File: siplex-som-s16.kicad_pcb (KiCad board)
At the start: 8 copper layers, 30 x 30 mm, 58 parts, among them J1 RFShield_OnePiece, J5 Conn_01x22, J7 Conn_01x22, J8 Conn_01x22, J9 Conn_01x22, U1 STM32H743IIKx, U2 IS42S16160J-6BLI, U3 W25Q32JVZP, U4 AP2112K-3.3, U5 W25Q32JVZP, Y1 25MHz, Y2 32.768KHz

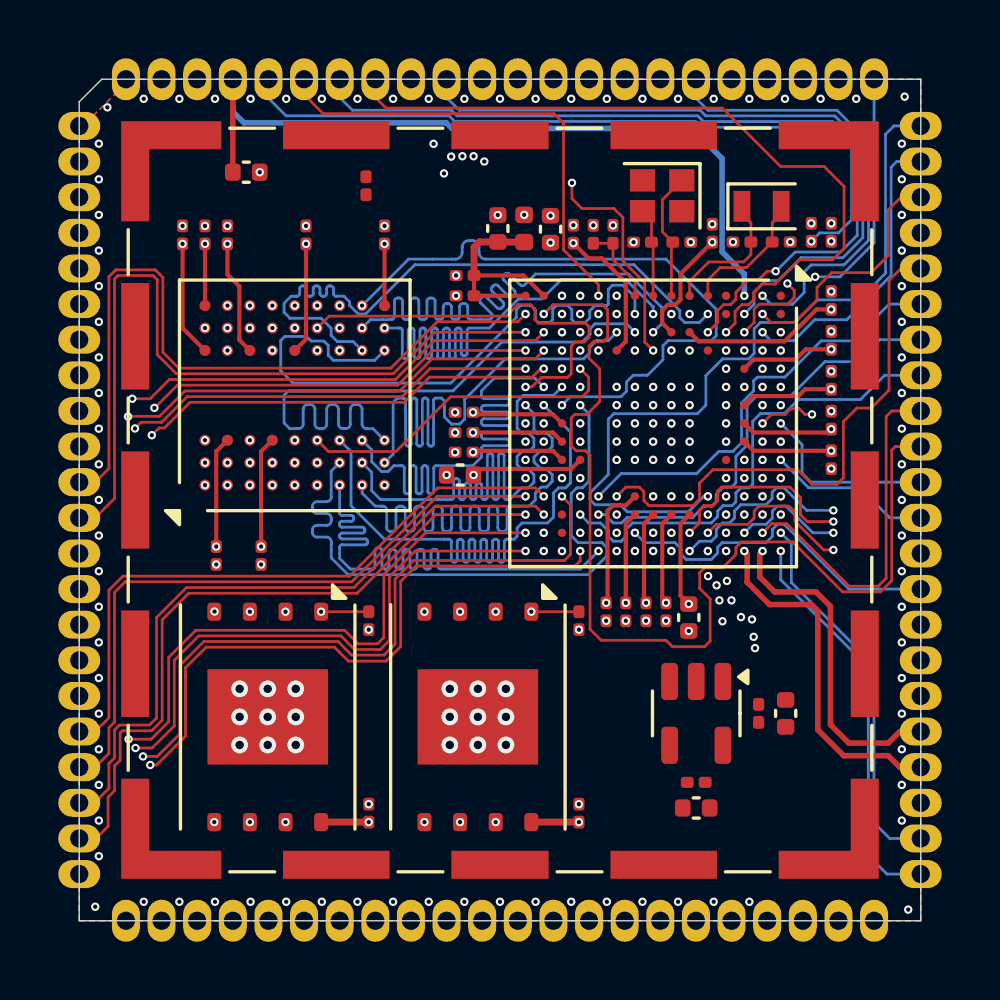
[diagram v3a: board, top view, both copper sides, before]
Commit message: Changed PMIC to dc-dc converter, finished track
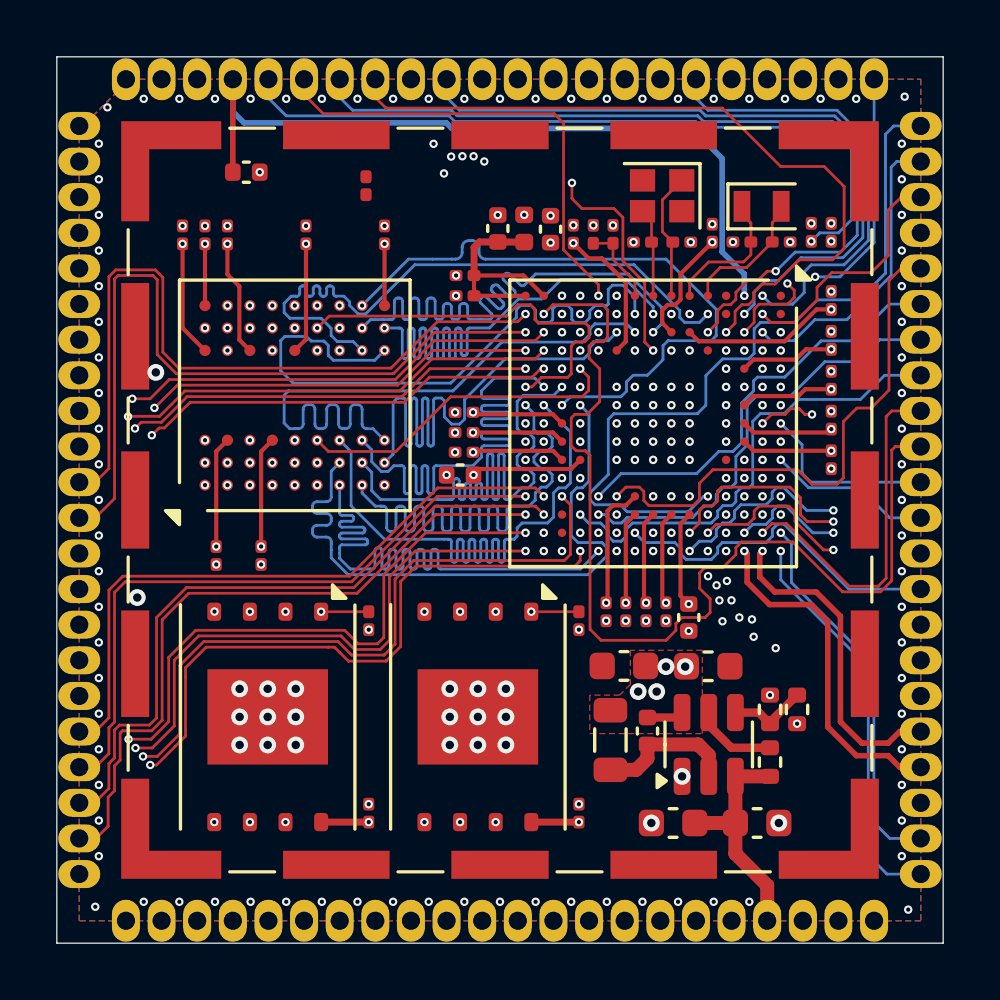
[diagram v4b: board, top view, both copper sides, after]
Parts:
- removed C35, C37: 100n, Capacitor_SMD:C_0201_0603Metric
- removed U4: AP2112K-3.3, Package_TO_SOT_SMD:SOT-23-5
- added C42: 10u, Capacitor_SMD:C_0603_1608Metric, F.Cu at (146.5, 109.6)
- added C43: 100n, Capacitor_SMD:C_0402_1005Metric, F.Cu at (145.6, 106.3)
- added C44: 22u, Capacitor_SMD:C_0603_1608Metric, F.Cu at (147.7, 104.0)
- added L2: 2u2, Inductor_SMD:L_0805_2012Metric, F.Cu at (144.2, 106.6)
- added R6: 10K, Resistor_SMD:R_0402_1005Metric, F.Cu at (149.9, 107.4)
- added R7: 33.2K, Resistor_SMD:R_0402_1005Metric, F.Cu at (149.9, 105.5)
- added R8: 10.0K, Resistor_SMD:R_0402_1005Metric, F.Cu at (150.9, 105.5)
- added U7: TPS562200, Package_TO_SOT_SMD:SOT-23-6, F.Cu at (147.8, 106.8)
- C34: value 2u2 -> 10u; footprint Capacitor_SMD:C_0402_1005Metric -> Capacitor_SMD:C_0603_1608Metric
- C36: value 1u -> 22u; footprint Capacitor_SMD:C_0402_1005Metric -> Capacitor_SMD:C_0603_1608Metric
- moved C36 5.68 mm to (144.7, 104.0)
- moved C34 4.04 mm to (149.5, 109.6), turned to 0 degrees
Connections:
- J9 pad 19: unconnected-(J9-Pin_19-Pad19) -> VIN
- J9 pad 20: unconnected-(J9-Pin_20-Pad20) -> +3V3
- J9 pad 21: unconnected-(J9-Pin_21-Pad21) -> GND
- J9 pad 22: unconnected-(J9-Pin_22-Pad22) -> GND
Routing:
- net PD7: track 23.8 -> 32.7 mm
- net PI3: track 18.2 -> 26.8 mm
- net VIN: track 0.00 -> 8.30 mm
- net PA15: track 18.1 -> 26.0 mm
- net PC12: track 19.0 -> 25.7 mm
- net Net-(U7-SW): track 0.00 -> 5.09 mm
- net PG11: track 22.3 -> 27.1 mm
- net Net-(U7-EN): track 0.00 -> 2.97 mm
- net Net-(U7-VFB): track 0.00 -> 2.82 mm
- net PB4: track 23.1 -> 25.2 mm
- net Net-(U7-VBST): track 0.00 -> 1.31 mm
- net /Castellated_holes/LTDC_R1: track 37.0 -> 36.3 mm
- net +3V3: vias 29 -> 34
- net GND: vias 186 -> 193
- added copper zone on F.Cu, net +3V3
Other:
- board size 30 x 30 mm -> 31.6 x 31.6 mm

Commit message: generate doc
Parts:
- added D1: BAT54CW, Package_TO_SOT_SMD:SOT-23, F.Cu at (136.2, 87.8)
- moved C15 22.9 mm to (151.0, 103.8)
- moved C10 7.39 mm to (138.4, 88.4), turned to 90 degrees
- moved C28 2.08 mm to (134.1, 88.6)
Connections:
- J7 pad 1: PB7 -> PB5
- J7 pad 2: PB5 -> GND
- J7 pad 3: GND -> VRTC
- J7 pad 4: VBAT -> /Castellated_holes/NRST
- J8 pad 1: PB8 -> PB7
- J8 pad 10: PA4 -> PA1
- J8 pad 11: PA3 -> PA4
- J8 pad 12: PA7 -> PA3
- J8 pad 13: PA6 -> PA7
- J8 pad 14: PA5 -> PA6
- J8 pad 15: PB0 -> PA5
- J8 pad 16: PB1 -> PB0
- J8 pad 17: PC5 -> PB1
- J8 pad 18: PB12 -> PC5
- J8 pad 19: PB10 -> PB12
- J8 pad 2: PB9 -> PB8
- J8 pad 20: PB13 -> PB10
- J8 pad 21: PB11 -> PB13
- J8 pad 22: PB14 -> PB11
- J8 pad 3: PH4 -> PB9
- J8 pad 4: GND -> PH4
- J8 pad 5: PC0 -> GND
- J8 pad 6: PC1 -> PC0
- J8 pad 7: PC4 -> PC1
- J8 pad 8: PA0 -> PC4
- J8 pad 9: PA1 -> PA0
- J9 pad 1: PB15 -> PB14
- J9 pad 2: PH7 -> PB15
- J9 pad 3: PD13 -> PH7
- J9 pad 4: PC6 -> PD13
- J9 pad 5: PC7 -> PC6
- J9 pad 6: PC8 -> PC7
- J9 pad 7: PH14 -> PC8
- J9 pad 8: GND -> PH14
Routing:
- net VRTC: track 0.00 -> 8.52 mm
- net VBAT: track 27.8 -> 23.9 mm, vias 1 -> 2
- net PB0: track 22.9 -> 25.4 mm
- net PB1: track 24.5 -> 26.9 mm
- net PC5: track 25.6 -> 27.8 mm
- net PH14: track 25.7 -> 24.1 mm
- net PB12: track 22.9 -> 24.5 mm, vias 1 -> 2
- net PB10: track 23.2 -> 24.5 mm, vias 1 -> 2
- net +3V3: track 80.5 -> 81.9 mm, vias 34 -> 35
- net PA4: track 30.7 -> 32.1 mm
- net PA1: track 29.9 -> 31.2 mm
- net PA7: track 27.7 -> 29.0 mm
- net PA3: track 26.9 -> 28.2 mm
- net PH4: track 28.0 -> 29.4 mm
- net PB5: track 38.1 -> 39.4 mm
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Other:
- board size 31.6 x 31.6 mm -> 30 x 30 mm

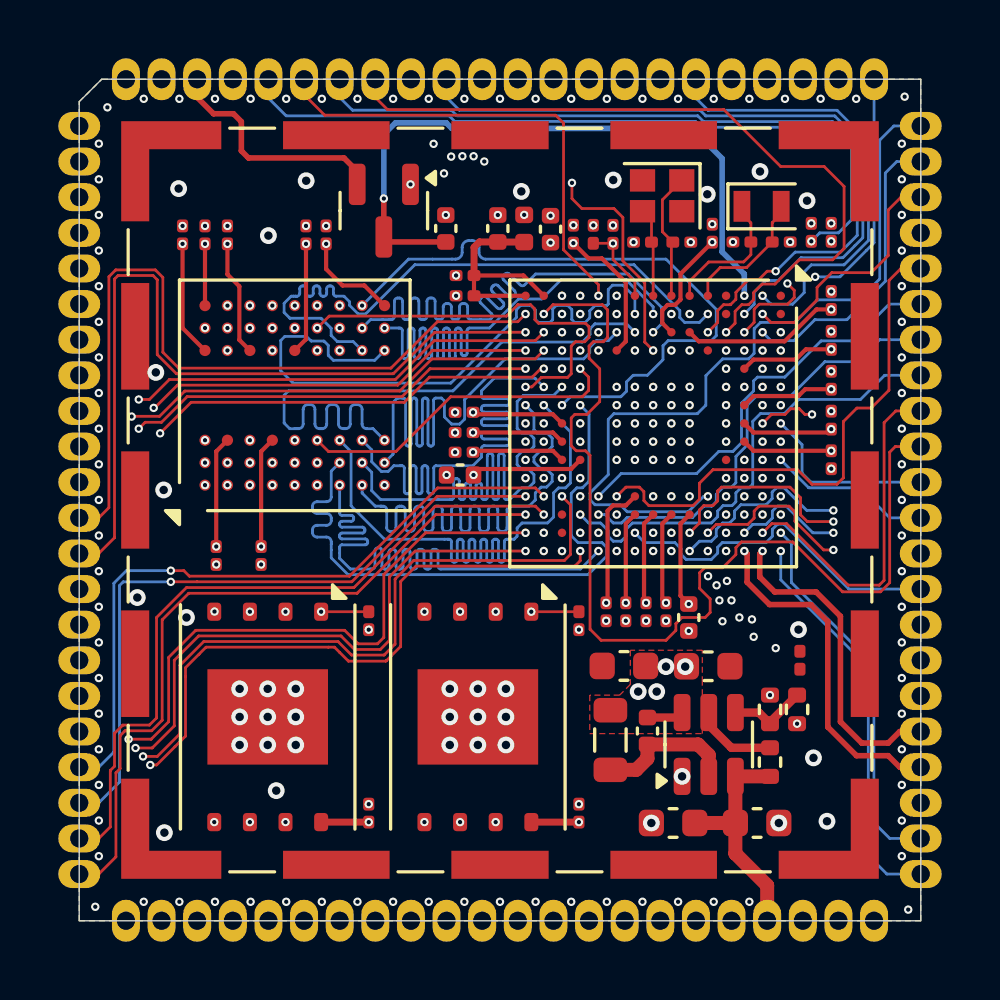
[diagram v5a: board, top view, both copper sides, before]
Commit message: Change LCD CLK, VSYNC, HSYNC, to be match with the position of standard 40 pin LCD module
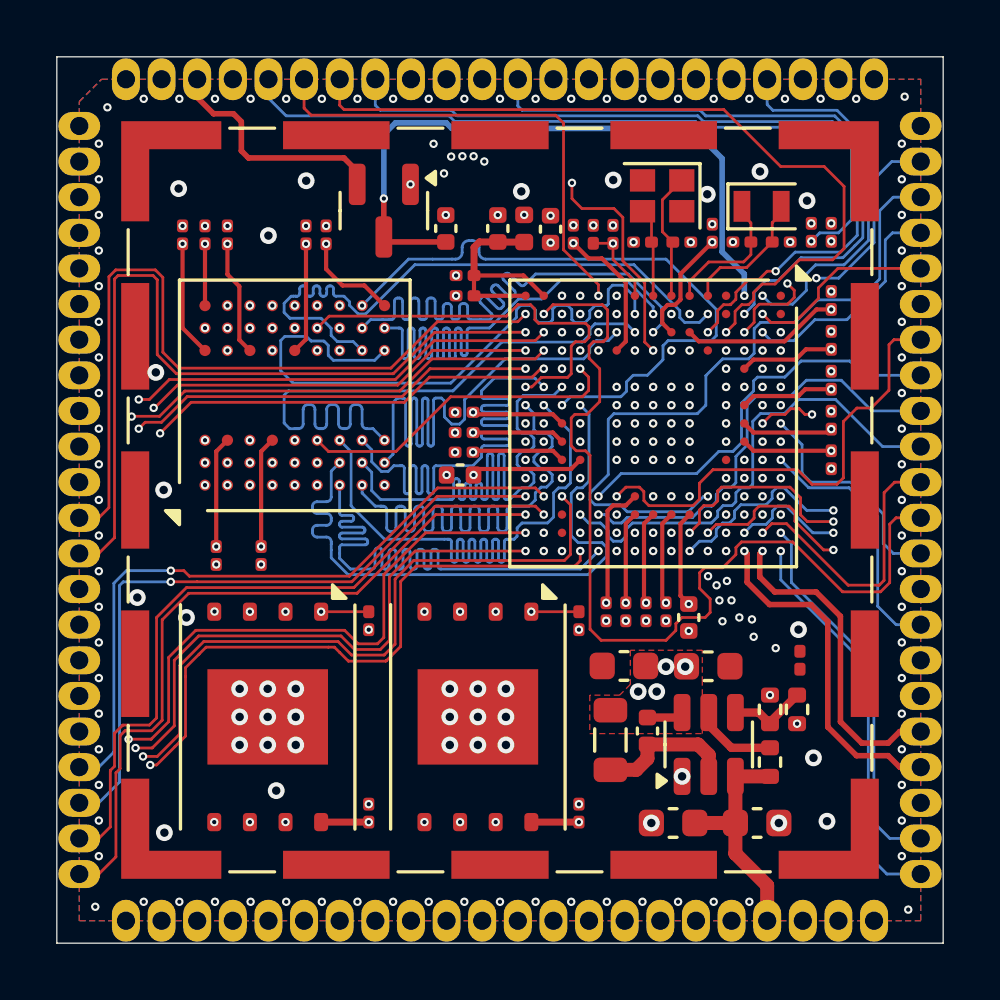
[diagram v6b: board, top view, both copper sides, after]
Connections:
- J5 pad 10: GND -> /Castellated_holes/LTDC_R0
- J5 pad 11: /Castellated_holes/SWO -> /Castellated_holes/LTDC_R1
- J5 pad 12: /Castellated_holes/LTDC_R0 -> /Castellated_holes/LTDC_R2
- J5 pad 13: /Castellated_holes/LTDC_R1 -> /Castellated_holes/LTDC_R3
- J5 pad 14: /Castellated_holes/LTDC_R2 -> /Castellated_holes/LTDC_R4
- J5 pad 15: /Castellated_holes/LTDC_R3 -> /Castellated_holes/LTDC_R5
- J5 pad 16: /Castellated_holes/LTDC_R4 -> /Castellated_holes/LTDC_R6
- J5 pad 17: /Castellated_holes/LTDC_R5 -> /Castellated_holes/LTDC_R7
- J5 pad 18: /Castellated_holes/LTDC_R6 -> /Castellated_holes/LTDC_G0
- J5 pad 19: /Castellated_holes/LTDC_R7 -> /Castellated_holes/LTDC_G1
- J5 pad 20: /Castellated_holes/LTDC_G0 -> /Castellated_holes/LTDC_G2
- J5 pad 21: /Castellated_holes/LTDC_G1 -> /Castellated_holes/LTDC_G3
- J5 pad 22: /Castellated_holes/LTDC_G2 -> /Castellated_holes/LTDC_G4
- J5 pad 8: GND -> /Castellated_holes/SWO
- J5 pad 9: /Castellated_holes/LTDC_CLK -> GND
- J7 pad 10: /Castellated_holes/LTDC_B7 -> /Castellated_holes/LTDC_CLK
- J7 pad 11: /Castellated_holes/LTDC_B6 -> GND
- J7 pad 12: /Castellated_holes/LTDC_B5 -> /Castellated_holes/LTDC_B7
- J7 pad 13: /Castellated_holes/LTDC_B4 -> /Castellated_holes/LTDC_B6
- J7 pad 14: /Castellated_holes/LTDC_B3 -> /Castellated_holes/LTDC_B5
- J7 pad 15: /Castellated_holes/LTDC_B2 -> /Castellated_holes/LTDC_B4
- J7 pad 16: /Castellated_holes/LTDC_B1 -> /Castellated_holes/LTDC_B3
- J7 pad 17: /Castellated_holes/LTDC_B0 -> /Castellated_holes/LTDC_B2
- J7 pad 18: /Castellated_holes/LTDC_G7 -> /Castellated_holes/LTDC_B1
- J7 pad 19: /Castellated_holes/LTDC_G6 -> /Castellated_holes/LTDC_B0
- J7 pad 20: /Castellated_holes/LTDC_G5 -> /Castellated_holes/LTDC_G7
- J7 pad 21: /Castellated_holes/LTDC_G4 -> /Castellated_holes/LTDC_G6
- J7 pad 22: /Castellated_holes/LTDC_G3 -> /Castellated_holes/LTDC_G5
- J7 pad 7: /Castellated_holes/LTDC_HSYNC -> /Castellated_holes/LTDC_VSYNC
- J7 pad 8: /Castellated_holes/LTDC_VSYNC -> /Castellated_holes/LTDC_HSYNC
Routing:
- net /Castellated_holes/LTDC_CLK: track 12.4 -> 40.9 mm
- net /Castellated_holes/SWO: track 5.85 -> 9.30 mm
- net /Castellated_holes/LTDC_B6: track 22.1 -> 19.4 mm
- net /Castellated_holes/LTDC_R1: track 36.3 -> 33.8 mm
- net /Castellated_holes/LTDC_B2: track 33.9 -> 31.4 mm
- net /Castellated_holes/LTDC_G2: track 27.2 -> 24.7 mm
- net /Castellated_holes/LTDC_R2: track 12.5 -> 10.0 mm
- net /Castellated_holes/LTDC_B0: track 16.3 -> 13.8 mm
- net /Castellated_holes/LTDC_B1: track 21.0 -> 18.6 mm
- net /Castellated_holes/LTDC_G1: track 10.7 -> 8.22 mm
- net /Castellated_holes/LTDC_B4: track 22.2 -> 19.8 mm
- net /Castellated_holes/LTDC_B3: track 32.4 -> 30.0 mm
- net /Castellated_holes/LTDC_B5: track 22.4 -> 20.0 mm
- net /Castellated_holes/LTDC_R6: track 19.2 -> 16.8 mm
- net /Castellated_holes/LTDC_R7: track 22.9 -> 20.5 mm
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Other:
- board size 30 x 30 mm -> 31.6 x 31.6 mm
